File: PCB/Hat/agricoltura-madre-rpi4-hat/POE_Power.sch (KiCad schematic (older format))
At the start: 19 parts, among them J1 Barrel_Jack, M2 AG9900M, SW2 EG1213, U1 AP7361C-33FGE-7

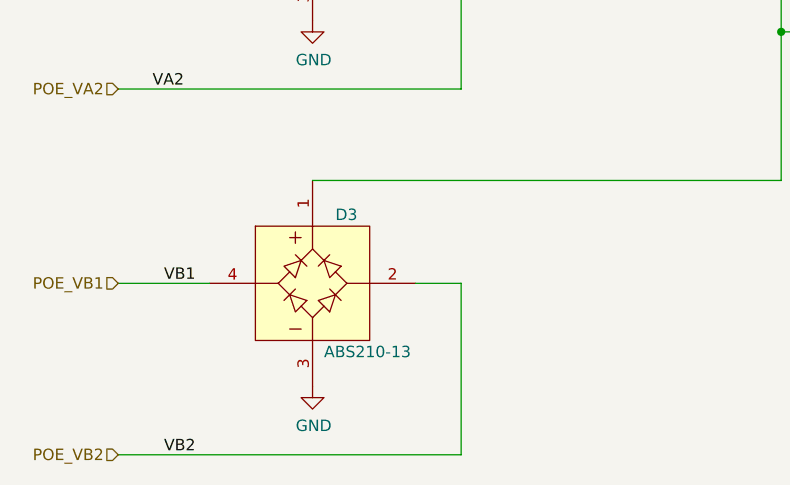
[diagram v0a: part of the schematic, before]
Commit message: RPi version PSU
updated POE circuit with fixed footprint for rectifier diodes.
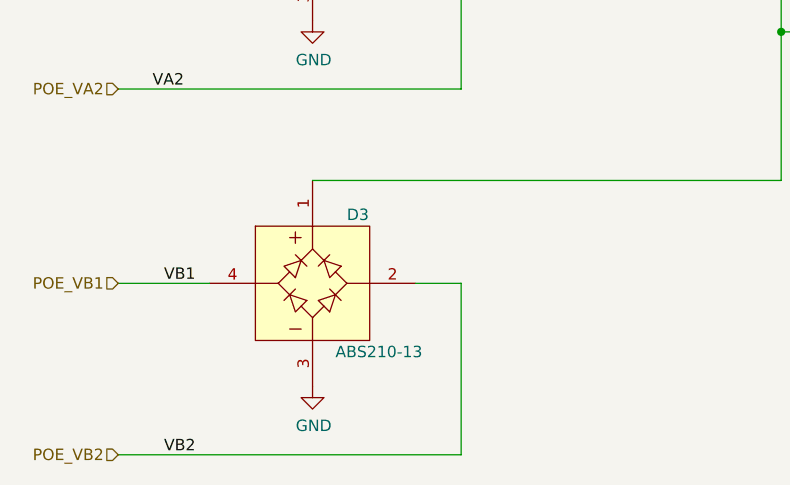
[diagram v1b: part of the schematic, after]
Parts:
- removed D2, D3: ABS210-13, growbox-KiCAD-Diodes:ABS210-13, symbol growbox-KiCAD-Diodes:ABS210-13
- added D2, D3: ABS210-13, AVR-KiCAD-Lib-Diodes:ABS210-13, symbol AVR-KiCAD-Lib-Diodes:ABS210-13
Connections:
- net +48V: now also D2.1, D3.1
- net GND: now also D2.3, D3.3
- net POE_VA1: now also D2.4
- net POE_VA2: now also D2.2
- net POE_VB1: now also D3.4
- net POE_VB2: now also D3.2
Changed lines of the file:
@@
 $EndComp
 Connection ~ 8050 2600
-$Comp
-L growbox-KiCAD-Diodes:ABS210-13 D2
-U 1 1 5E988607
-P 1750 4750
-F 0 "D2" H 2100 4800 50  0000 L CNN
-F 1 "ABS210-13" H 2000 5600 50  0001 C CNN
-F 2 "growbox-KiCAD-Diodes:ABS210-13" V 2150 4650 50  0001 C CNN
-F 3 "https://www.comchiptech.com/admin/files/product/20190215095655.pdf" H 1750 4800 50  0001 C CNN
-F 4 "0.45000" H 2050 5650 50  0001 C CNN "Cost QTY: 1"
-F 5 "0.10988" H 2150 5750 50  0001 C CNN "Cost QTY: 1000"
-F 6 "0.10054" H 2250 5850 50  0001 C CNN "Cost QTY: 2500"
-F 7 "0.09615" H 2350 5950 50  0001 C CNN "Cost QTY: 5000"
-F 8 "0.08516" H 2450 6050 50  0001 C CNN "Cost QTY: 10000"
-F 9 "Diodes Incorporated" H 2550 6150 50  0001 C CNN "MFR"
-F 10 "ABS210-13" H 2650 6250 50  0001 C CNN "MFR#"
-F 11 "Digikey" H 2750 6350 50  0001 C CNN "Vendor"
-F 12 "ABS210-13DICT-ND" H 2850 6450 50  0001 C CNN "Vendor #"
-F 13 "AVR" H 2950 6550 50  0001 C CNN "Designer"
-F 14 "2.6mm" H 3050 6650 50  0001 C CNN "Height"
-F 15 "3/23/2020" H 4150 7750 50  0001 C CNN "Date Created"
-F 16 "4/12/2020" H 3150 6750 50  0001 C CNN "Date Modified"
-F 17 "Yes" H 3250 6850 50  0001 C CNN "Lead-Free ?"
-F 18 "1" H 3350 6950 50  0001 C CNN "RoHS Levels"
-F 19 "SMT" H 3450 7050 50  0001 C CNN "Mounting"
-F 20 "4" H 3550 7150 50  0001 C CNN "Pin Count #"
-F 21 "Active" H 3650 7250 50  0001 C CNN "Status"
-F 22 "*" H 3750 7350 50  0001 C CNN "Tolerance"
-F 23 "Rectifier Diode" H 3850 7450 50  0001 C CNN "Type"
-F 24 "1KV 2A" H 3950 7550 50  0001 C CNN "Voltage"
-F 25 "4-SOPA" H 4050 7700 50  0001 C CNN "Package"
-F 26 "Bridge Rectifier Single Phase Standard 1kV Surface Mount 4-SOPA" H 4350 8000 50  0001 C CNN "Description"
-F 27 "ABS210-13" H 2050 4200 50  0000 L CNN "_Value_"
-F 28 "*" H 4350 8000 50  0001 C CNN "Management_ID"
-	1    1750 4750
-	1    0    0    -1
-$EndComp
 Wire Wire Line
 	1150 5000 1550 5000
@@
 F 3 "" H 2000 5450 50  0001 C CNN
 	1    2000 5450
-	1    0    0    -1
-$EndComp
-$Comp
-L growbox-KiCAD-Diodes:ABS210-13 D3
-U 1 1 5E99C1D3
-P 1750 6350
-F 0 "D3" H 2100 6400 50  0000 L CNN
-F 1 "ABS210-13" H 2000 7200 50  0001 C CNN
-F 2 "growbox-KiCAD-Diodes:ABS210-13" V 2150 6250 50  0001 C CNN
-F 3 "https://www.comchiptech.com/admin/files/product/20190215095655.pdf" H 1750 6400 50  0001 C CNN
-F 4 "0.45000" H 2050 7250 50  0001 C CNN "Cost QTY: 1"
-F 5 "0.10988" H 2150 7350 50  0001 C CNN "Cost QTY: 1000"
-F 6 "0.10054" H 2250 7450 50  0001 C CNN "Cost QTY: 2500"
-F 7 "0.09615" H 2350 7550 50  0001 C CNN "Cost QTY: 5000"
-F 8 "0.08516" H 2450 7650 50  0001 C CNN "Cost QTY: 10000"
-F 9 "Diodes Incorporated" H 2550 7750 50  0001 C CNN "MFR"
-F 10 "ABS210-13" H 2650 7850 50  0001 C CNN "MFR#"
-F 11 "Digikey" H 2750 7950 50  0001 C CNN "Vendor"
-F 12 "ABS210-13DICT-ND" H 2850 8050 50  0001 C CNN "Vendor #"
-F 13 "AVR" H 2950 8150 50  0001 C CNN "Designer"
-F 14 "2.6mm" H 3050 8250 50  0001 C CNN "Height"
-F 15 "3/23/2020" H 4150 9350 50  0001 C CNN "Date Created"
-F 16 "4/12/2020" H 3150 8350 50  0001 C CNN "Date Modified"
-F 17 "Yes" H 3250 8450 50  0001 C CNN "Lead-Free ?"
-F 18 "1" H 3350 8550 50  0001 C CNN "RoHS Levels"
-F 19 "SMT" H 3450 8650 50  0001 C CNN "Mounting"
-F 20 "4" H 3550 8750 50  0001 C CNN "Pin Count #"
-F 21 "Active" H 3650 8850 50  0001 C CNN "Status"
-F 22 "*" H 3750 8950 50  0001 C CNN "Tolerance"
-F 23 "Rectifier Diode" H 3850 9050 50  0001 C CNN "Type"
-F 24 "1KV 2A" H 3950 9150 50  0001 C CNN "Voltage"
-F 25 "4-SOPA" H 4050 9300 50  0001 C CNN "Package"
-F 26 "Bridge Rectifier Single Phase Standard 1kV Surface Mount 4-SOPA" H 4350 9600 50  0001 C CNN "Description"
-F 27 "ABS210-13" H 2050 5800 50  0000 L CNN "_Value_"
-F 28 "*" H 4350 9600 50  0001 C CNN "Management_ID"
-	1    1750 6350
 	1    0    0    -1
 $EndComp
@@
 Wire Wire Line
 	9150 4450 9150 4350
+$Comp
+L AVR-KiCAD-Lib-Diodes:ABS210-13 D2
+U 1 1 5F063034
+P 1750 4750
+F 0 "D2" H 2100 4800 50  0000 L CNN
+F 1 "ABS210-13" H 2000 5600 50  0001 C CNN
+F 2 "AVR-KiCAD-Lib-Diodes:ABS210-13" V 2150 4650 50  0001 C CNN
+F 3 "https://www.comchiptech.com/admin/files/product/20190215095655.pdf" H 1750 4800 50  0001 C CNN
+F 4 "0.45000" H 2050 5650 50  0001 C CNN "Cost QTY: 1"
+F 5 "0.10988" H 2150 5750 50  0001 C CNN "Cost QTY: 1000"
+F 6 "0.10054" H 2250 5850 50  0001 C CNN "Cost QTY: 2500"
+F 7 "0.09615" H 2350 5950 50  0001 C CNN "Cost QTY: 5000"
+F 8 "0.08516" H 2450 6050 50  0001 C CNN "Cost QTY: 10000"
+F 9 "Diodes Incorporated" H 2550 6150 50  0001 C CNN "MFR"
+F 10 "ABS210-13" H 2650 6250 50  0001 C CNN "MFR#"
+F 11 "Digikey" H 2750 6350 50  0001 C CNN "Vendor"
+F 12 "ABS210-13DICT-ND" H 2850 6450 50  0001 C CNN "Vendor #"
+F 13 "AVR" H 2950 6550 50  0001 C CNN "Designer"
+F 14 "2.6mm" H 3050 6650 50  0001 C CNN "Height"
+F 15 "3/23/2020" H 4150 7750 50  0001 C CNN "Date Created"
+F 16 "4/12/2020" H 3150 6750 50  0001 C CNN "Date Modified"
+F 17 "Yes" H 3250 6850 50  0001 C CNN "Lead-Free ?"
+F 18 "1" H 3350 6950 50  0001 C CNN "RoHS Levels"
+F 19 "SMT" H 3450 7050 50  0001 C CNN "Mounting"
+F 20 "4" H 3550 7150 50  0001 C CNN "Pin Count #"
+F 21 "Active" H 3650 7250 50  0001 C CNN "Status"
+F 22 "*" H 3750 7350 50  0001 C CNN "Tolerance"
+F 23 "Rectifier Diode" H 3850 7450 50  0001 C CNN "Type"
+F 24 "1KV 2A" H 3950 7550 50  0001 C CNN "Voltage"
+F 25 "4-SOPA" H 4050 7700 50  0001 C CNN "Package"
+F 26 "Bridge Rectifier Single Phase Standard 1kV Surface Mount 4-SOPA" H 4350 8000 50  0001 C CNN "Description"
+F 27 "ABS210-13" H 2050 4200 50  0000 L CNN "_Value_"
+F 28 "*" H 4350 8000 50  0001 C CNN "Management_ID"
+	1    1750 4750
+	1    0    0    -1
+$EndComp
+$Comp
+L AVR-KiCAD-Lib-Diodes:ABS210-13 D3
+U 1 1 5F064D69
+P 1750 6350
+F 0 "D3" H 2150 6400 50  0000 L CNN
+F 1 "ABS210-13" H 2000 7200 50  0001 C CNN
+F 2 "AVR-KiCAD-Lib-Diodes:ABS210-13" V 2150 6250 50  0001 C CNN
+F 3 "https://www.comchiptech.com/admin/files/product/20190215095655.pdf" H 1750 6400 50  0001 C CNN
+F 4 "0.45000" H 2050 7250 50  0001 C CNN "Cost QTY: 1"
+F 5 "0.10988" H 2150 7350 50  0001 C CNN "Cost QTY: 1000"
+F 6 "0.10054" H 2250 7450 50  0001 C CNN "Cost QTY: 2500"
+F 7 "0.09615" H 2350 7550 50  0001 C CNN "Cost QTY: 5000"
+F 8 "0.08516" H 2450 7650 50  0001 C CNN "Cost QTY: 10000"
+F 9 "Diodes Incorporated" H 2550 7750 50  0001 C CNN "MFR"
+F 10 "ABS210-13" H 2650 7850 50  0001 C CNN "MFR#"
+F 11 "Digikey" H 2750 7950 50  0001 C CNN "Vendor"
+F 12 "ABS210-13DICT-ND" H 2850 8050 50  0001 C CNN "Vendor #"
+F 13 "AVR" H 2950 8150 50  0001 C CNN "Designer"
+F 14 "2.6mm" H 3050 8250 50  0001 C CNN "Height"
+F 15 "3/23/2020" H 4150 9350 50  0001 C CNN "Date Created"
+F 16 "4/12/2020" H 3150 8350 50  0001 C CNN "Date Modified"
+F 17 "Yes" H 3250 8450 50  0001 C CNN "Lead-Free ?"
+F 18 "1" H 3350 8550 50  0001 C CNN "RoHS Levels"
+F 19 "SMT" H 3450 8650 50  0001 C CNN "Mounting"
+F 20 "4" H 3550 8750 50  0001 C CNN "Pin Count #"
+F 21 "Active" H 3650 8850 50  0001 C CNN "Status"
+F 22 "*" H 3750 8950 50  0001 C CNN "Tolerance"
+F 23 "Rectifier Diode" H 3850 9050 50  0001 C CNN "Type"
+F 24 "1KV 2A" H 3950 9150 50  0001 C CNN "Voltage"
+F 25 "4-SOPA" H 4050 9300 50  0001 C CNN "Package"
+F 26 "Bridge Rectifier Single Phase Standard 1kV Surface Mount 4-SOPA" H 4350 9600 50  0001 C CNN "Description"
+F 27 "ABS210-13" H 2100 5800 50  0000 L CNN "_Value_"
+F 28 "*" H 4350 9600 50  0001 C CNN "Management_ID"
+	1    1750 6350
+	1    0    0    -1
+$EndComp
 $EndSCHEMATC
